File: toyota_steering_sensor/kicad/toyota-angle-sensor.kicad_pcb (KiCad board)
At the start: 2 copper layers, 34.8 x 34.8 mm, 32 parts, among them IC1 ATMEGA328PB-AU, IC2 LS7366R, IC3 AS5047P, J1 AVR-ISP-6, J2 RJ45, U1 NCP1117-5.0_SOT223, U2 MCP2515, U3 TJA1050, Y1 16MHz, Y2 40MHz, Y3 8MHz

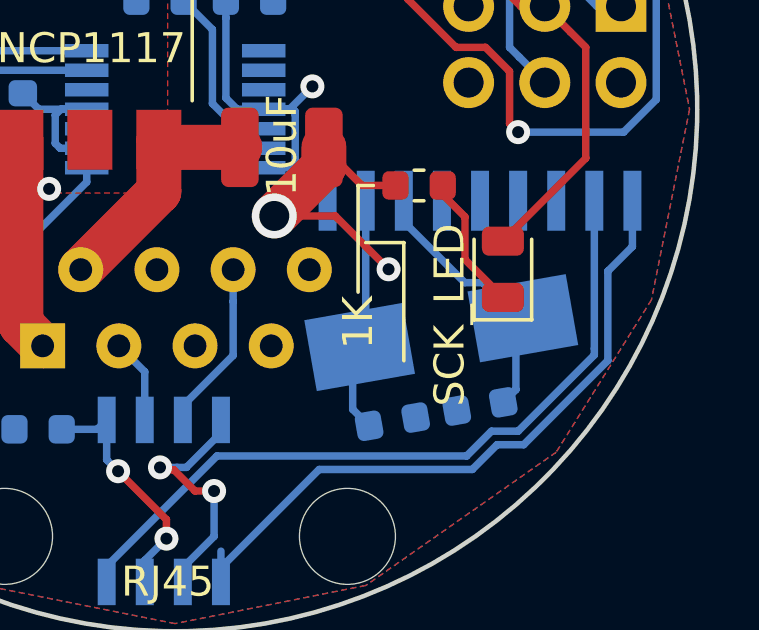
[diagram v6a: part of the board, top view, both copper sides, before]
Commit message: modified component ref for BOM
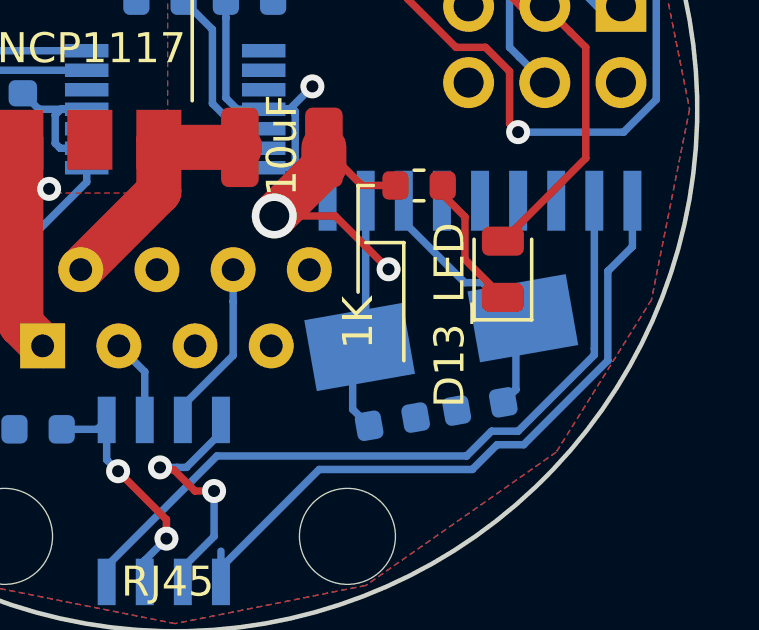
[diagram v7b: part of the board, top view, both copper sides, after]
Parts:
- C7: value 1.0uF -> 1uF
- D2: value SCK_LED -> D13_LED
- U4: renamed from U2; value MCP2515 -> MCP2515-xSO
- U6: renamed from U3; value TJA1050 -> TJA1051T-3
- renumbered IC1 to U2, IC2 to U3, IC3 to U5

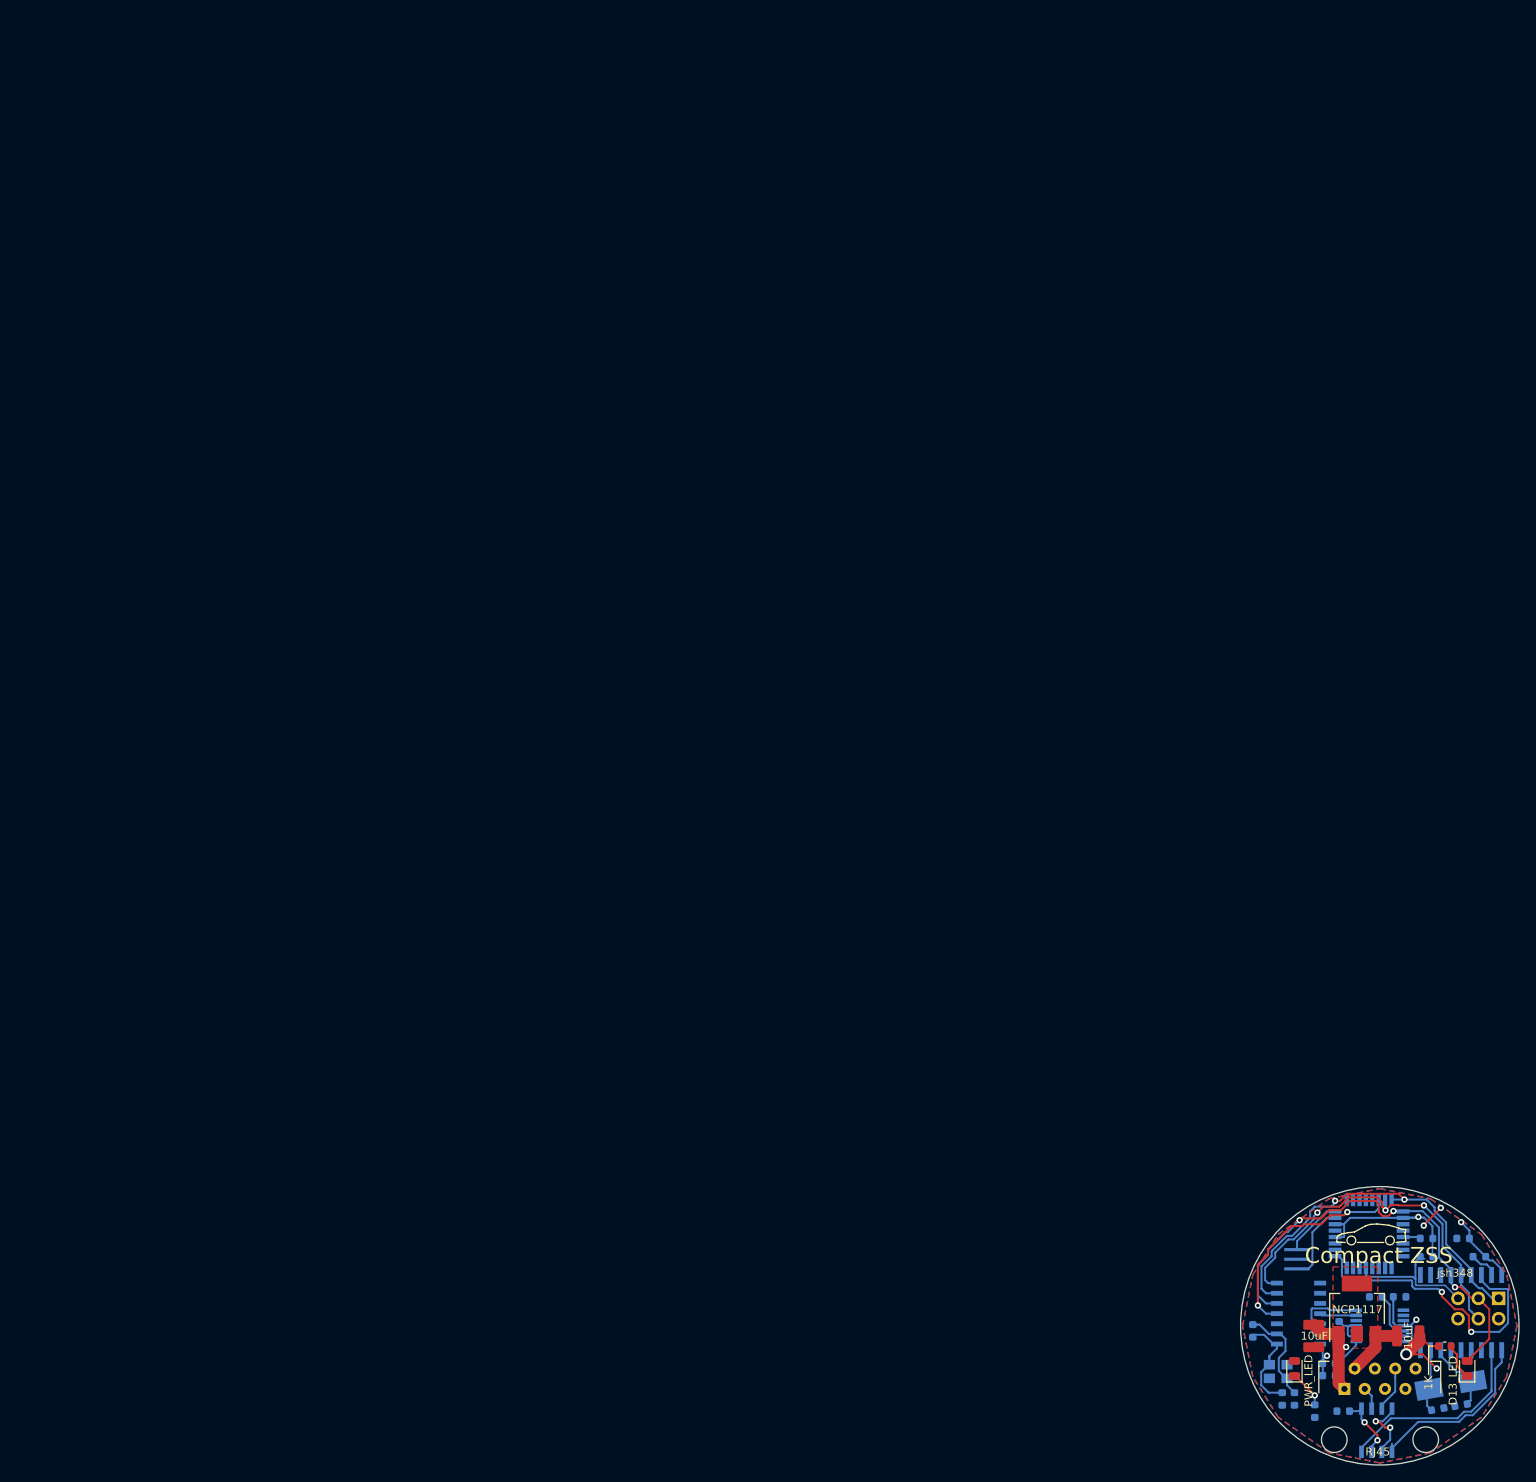
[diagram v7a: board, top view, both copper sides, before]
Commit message: shrink and re-route pcb. not done yet
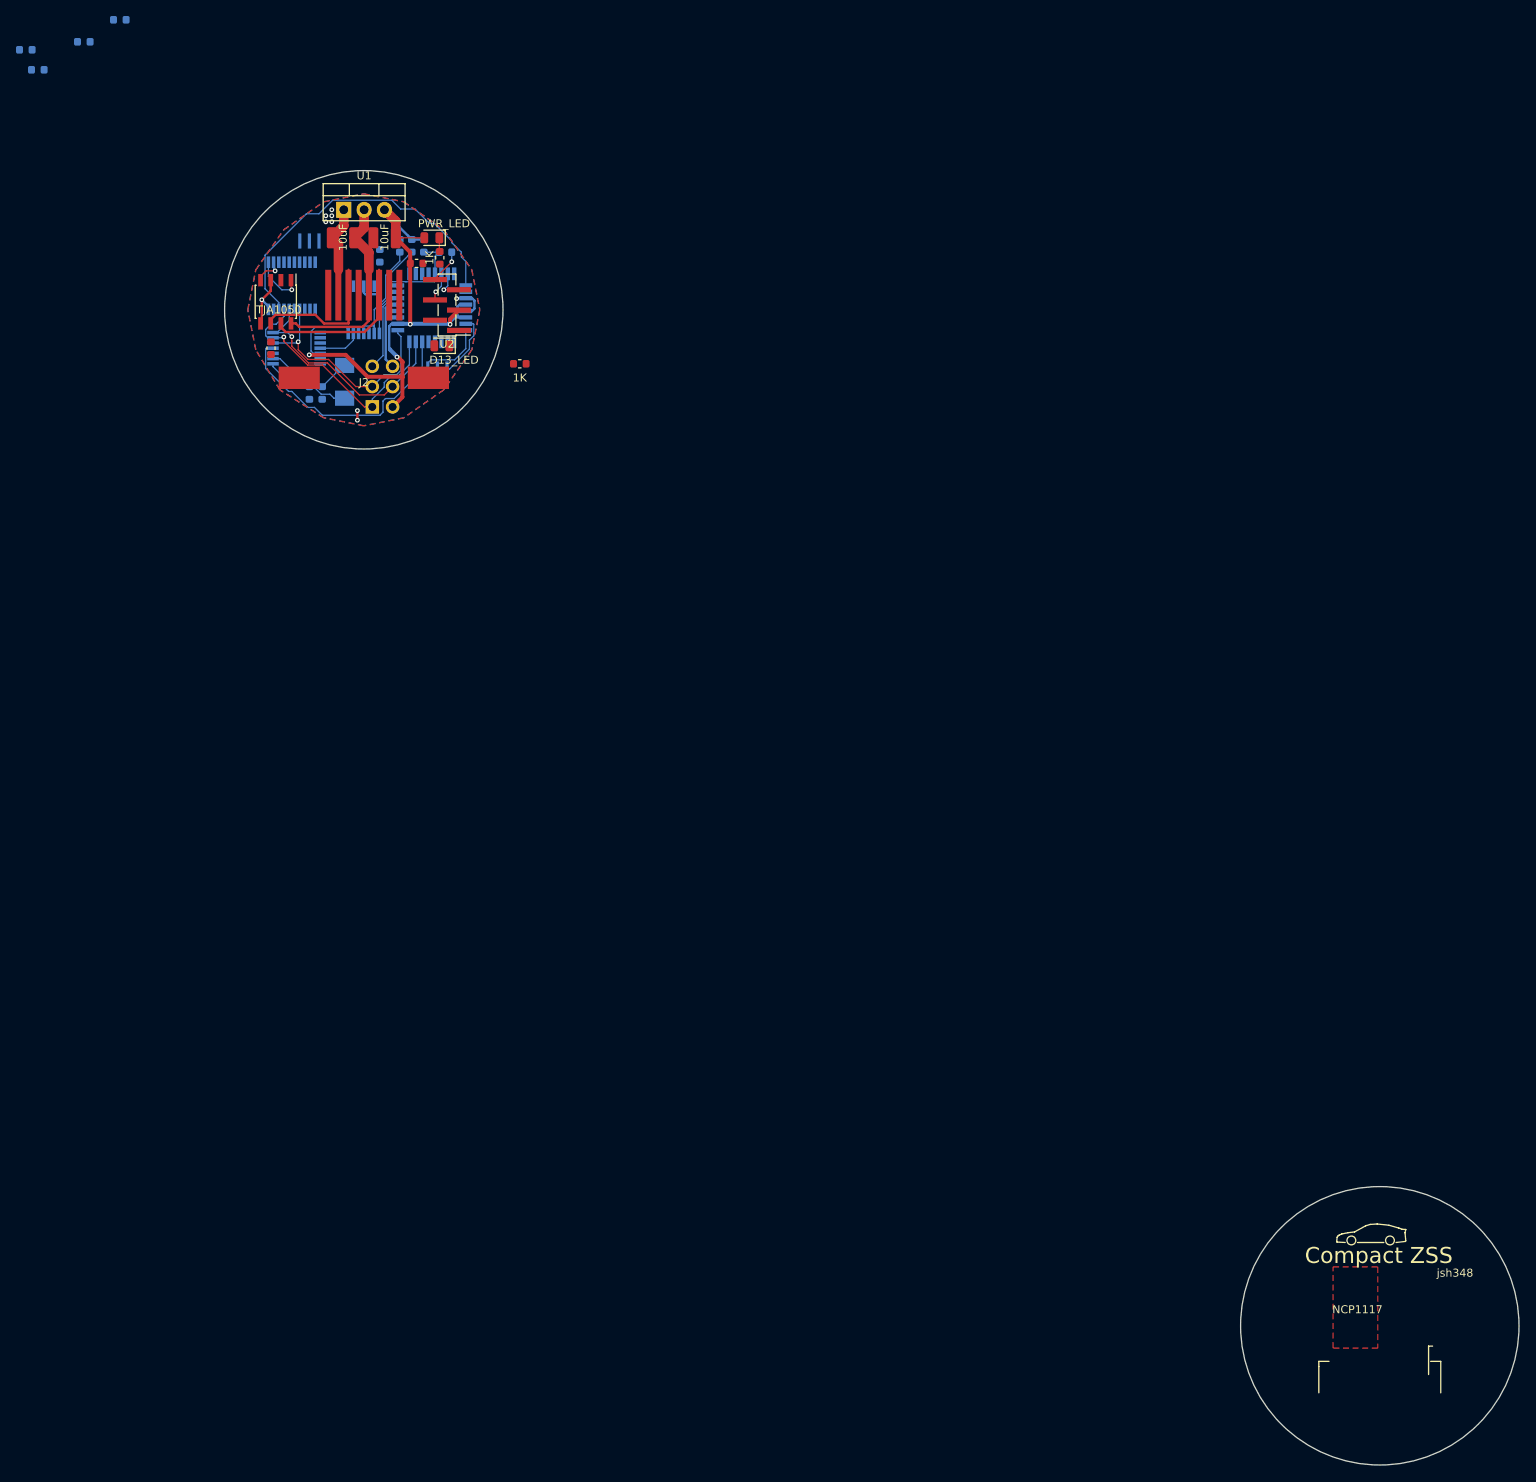
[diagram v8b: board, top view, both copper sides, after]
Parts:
- removed C6: 27pF, Capacitor_SMD:C_0603_1608Metric
- added IC1: ATMEGA328P-AU, Package_QFP:TQFP-32_7x7mm_P0.8mm, B.Cu at (8.50, -0.25)
- C5: value 27pF -> .1uF
- C8, R2, R5: moved to F.Cu
- J1: moved to B.Cu
- J2: footprint Connector_RJ:RJ45_Amphenol_54602-x08_Horizontal -> ZSS:Molex 855025008 RJ45
- U1: value NCP1117-5.0_SOT223 -> LM7805_TO220; footprint Package_TO_SOT_SMD:SOT-223-3_TabPin2 -> Package_TO_SOT_THT:TO-220-3_Vertical
- U2: value ATMEGA328PB-AU -> FTDI; footprint Package_QFP:TQFP-32_7x7mm_P0.8mm -> Connector_PinHeader_1.27mm:PinHeader_1x06_P1.27mm_Vertical_SMD_Pin1Left; moved to F.Cu
- U3: footprint Package_SO:SOIC-14_3.9x8.7mm_P1.27mm -> Package_SO:TSSOP-14_4.4x5mm_P0.65mm
- U4: value MCP2515-xSO -> MCP2515-xST; footprint Package_SO:SOIC-18W_7.5x11.6mm_P1.27mm -> Package_SO:TSSOP-20_4.4x6.5mm_P0.65mm
- U6: value TJA1051T-3 -> TJA1050; moved to F.Cu
- Y1: footprint Crystal:Resonator_SMD_muRata_CSTxExxV-3Pin_3.0x1.1mm_HandSoldering -> Crystal:Resonator_SMD_muRata_CSTxExxV-3Pin_3.0x1.1mm
- Y2: footprint Crystal:Crystal_SMD_Abracon_ABM8G-4Pin_3.2x2.5mm -> Crystal:Crystal_SMD_Abracon_ABM3-2Pin_5.0x3.2mm
- Y3: value 8MHz -> 20MHz; footprint Crystal:Crystal_SMD_Abracon_ABM3-2Pin_5.0x3.2mm_HandSoldering -> Crystal:Resonator_SMD_muRata_CSTxExxV-3Pin_3.0x1.1mm
- moved C10 233.1 mm to (-42.2, -32.5)
- moved C11 232.6 mm to (-35.0, -33.5)
- moved C12 229.1 mm to (-40.8, -30.0)
- moved C9 227.1 mm to (-30.5, -36.2)
- moved Y3 202.0 mm to (-6.80, -8.60), turned to 0 degrees
- moved U6 197.1 mm to (-11.0, -1.00), turned to 270 degrees
- moved U4 194.5 mm to (-9.00, -3.00), turned to 270 degrees
- moved C5 192.1 mm to (10.2, -7.20), turned to 0 degrees
- moved C1 191.2 mm to (-2.60, -9.00)
- moved R5 189.0 mm to (-11.6, 4.80), turned to 270 degrees
- moved U1 186.8 mm to (-2.50, -12.5), turned to 0 degrees
- moved J2 186.0 mm to (0.00, -5.00)
- moved D2 181.0 mm to (9.75, 4.50), turned to 180 degrees
- moved R2 181.0 mm to (9.50, -6.50)
- moved R6 180.7 mm to (6.00, -8.00), turned to 270 degrees
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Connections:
- C5 pad 1: Net-(C5-Pad1) -> /RESET
- C5 pad 2: GND -> /DTR
- J2 pad 4: Net-(J2-Pad4) -> (no net)
- J2 pad 7: Net-(J2-Pad7) -> (no net)
- J2 pad 8: Net-(J2-Pad8) -> (no net)
- U1 pad 1: GND -> +12V
- U1 pad 2: +5V -> GND
- U1 pad 3: +12V -> +5V
- U2 pad 1: /D3 -> GND
- U2 pad 2: Net-(U2-Pad2) -> GND
- U2 pad 3: GND -> +5V
- U2 pad 4: +5V -> Net-(IC1-Pad30)
- U2 pad 5: GND -> Net-(IC1-Pad31)
- U2 pad 6: +5V -> /DTR
- U3 pad 10: Net-(U3-Pad10) -> (no net)
- U3 pad 13: Net-(U3-Pad13) -> (no net)
- U3 pad 8: Net-(U3-Pad8) -> (no net)
- U3 pad 9: Net-(U3-Pad9) -> (no net)
- U4 pad 10: Net-(U4-Pad10) -> GND
- U4 pad 11: Net-(U4-Pad11) -> (no net)
- U4 pad 12: Net-(U4-Pad12) -> (no net)
- U4 pad 13: /D13,SCK -> (no net)
- U4 pad 14: /D11,MOSI -> /D13,SCK
- U4 pad 15: /D12,MISO -> (no net)
- U4 pad 16: /D3 -> /D11,MOSI
- U4 pad 17: Net-(R5-Pad2) -> /D12,MISO
- U4 pad 18: +5V -> /D3
- U4 pad 3: Net-(U4-Pad3) -> (no net)
- U4 pad 4: Net-(U4-Pad4) -> (no net)
- U4 pad 5: Net-(U4-Pad5) -> (no net)
- U4 pad 6: Net-(U4-Pad6) -> (no net)
- U4 pad 7: Net-(C5-Pad1) -> (no net)
- U4 pad 9: GND -> Net-(U4-Pad9)
- U5 pad 10: Net-(U5-Pad10) -> (no net)
- U5 pad 3: Net-(U5-Pad3) -> (no net)
- U5 pad 5: Net-(U5-Pad5) -> (no net)
- U5 pad 8: Net-(U5-Pad8) -> (no net)
- U5 pad 9: Net-(U5-Pad9) -> (no net)
- Y1 pad 1: Net-(U2-Pad8) -> Net-(IC1-Pad8)
- Y1 pad 3: Net-(U2-Pad7) -> Net-(IC1-Pad7)
- Y2 pad 2: Net-(Y2-Pad2) -> Net-(C4-Pad1)
- Y3 pad 2: Net-(C5-Pad1) -> GND
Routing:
- net /D13,SCK: track 56.5 -> 29.1 mm, vias 3 -> 1
- net +5V: track 54.5 -> 77.0 mm, vias 6 -> 5
- net Net-(U4-Pad2): track 24.8 -> 3.74 mm, vias 0 -> 1
- net /D11,MOSI: track 47.1 -> 30.1 mm, vias 3 -> 1
- net /D12,MISO: track 49.1 -> 32.6 mm, vias 2 -> 1
- net Net-(U4-Pad1): track 22.9 -> 6.63 mm, vias 0 -> 1
- net /CANL: track 2.83 -> 17.6 mm
- net /CANH: track 5.70 -> 19.7 mm
- net Net-(U2-Pad7): track 9.78 -> 0.00 mm
- net Net-(C5-Pad1): track 8.79 -> 0.00 mm
- net Net-(IC1-Pad8): track 0.00 -> 8.55 mm
- net Net-(IC1-Pad7): track 0.00 -> 8.19 mm
- net Net-(R7-Pad1): track 5.54 -> 13.7 mm
- net Net-(U4-Pad8): track 7.91 -> 0.00 mm
- net Net-(R6-Pad2): track 3.98 -> 11.8 mm
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- added copper zone on F.Cu, net GND
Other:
- board size 34.8 x 34.8 mm -> 161.8 x 161.8 mm
- net class Default: clearance 0.2 -> 0.13; trace_width 0.25 -> 0.13; via_dia 0.8 -> 0.6; via_drill 0.4 -> 0.3
- rule trace_clearance: 0.2 -> 0.13
- rule trace_min: 0.2 -> 0.13
- rule via_min_size: 0.4 -> 0.6
